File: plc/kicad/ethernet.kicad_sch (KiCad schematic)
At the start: 26 parts, among them U20 W5500, X1 X322525MRB4SI

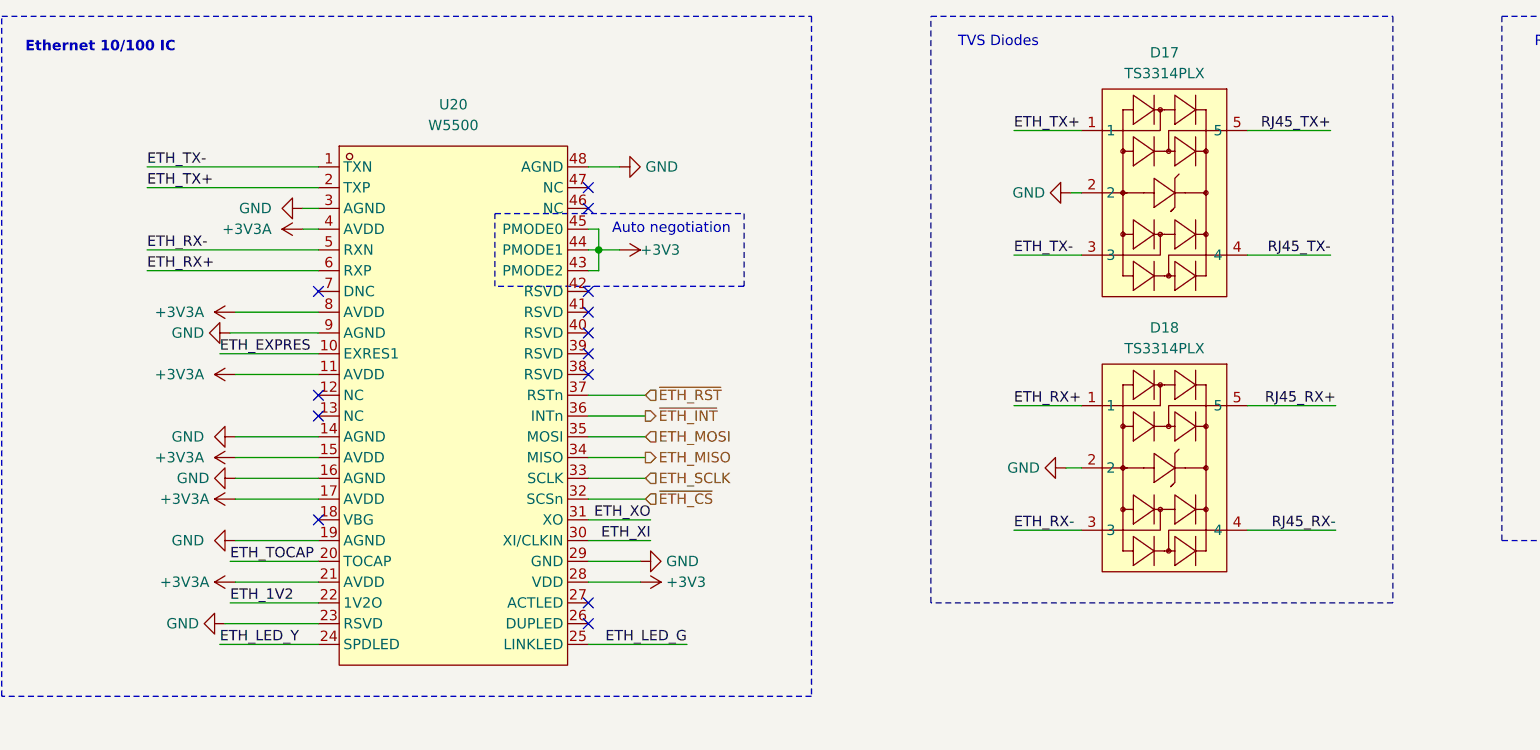
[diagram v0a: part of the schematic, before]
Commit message: Corrected TVS duplicated
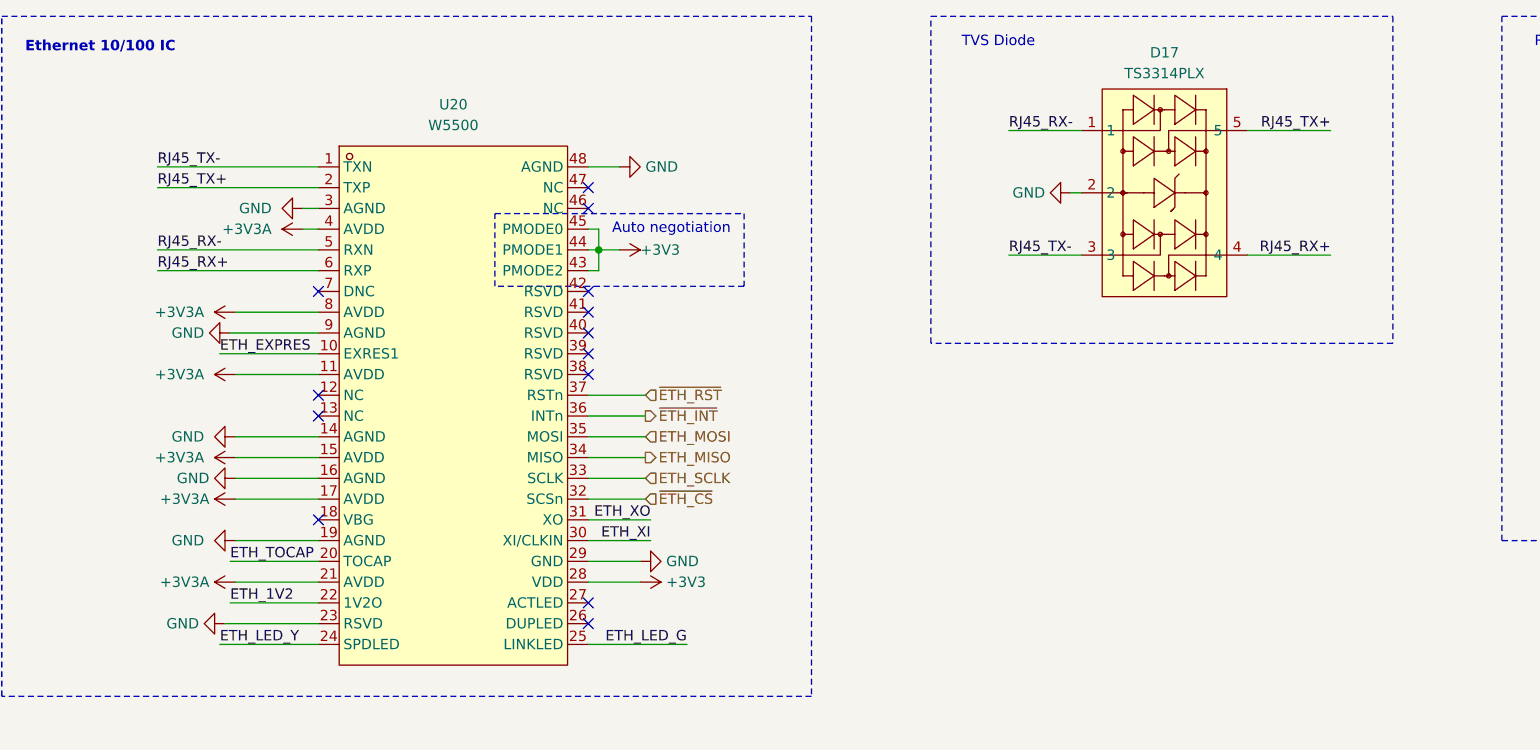
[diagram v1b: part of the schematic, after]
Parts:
- removed D18: TS3314PLX, LibrePLC32:SOT-23-5_L2.9-W1.6-P0.95-LS2.8-BR, symbol LibrePLC32:TS3314PLX
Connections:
- net ETH_RX+ is gone; now on net RJ45_RX+: U20.6 (RXP)
- net ETH_RX- is gone; now on net RJ45_RX-: U20.5 (RXN)
- net ETH_TX- is gone; now on net RJ45_TX-: D17.3, U20.1 (TXN)
- net RJ45_RX+: now also D17.4
- net RJ45_RX-: now also D17.1
- net RJ45_TX+: now also U20.2 (TXP)
- net RJ45_TX-: no longer D17.4
- removed net ETH_TX+: D17.1, U20.2 (TXP)
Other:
- note added: "TVS Diode"
- note removed: "TVS Diodes"

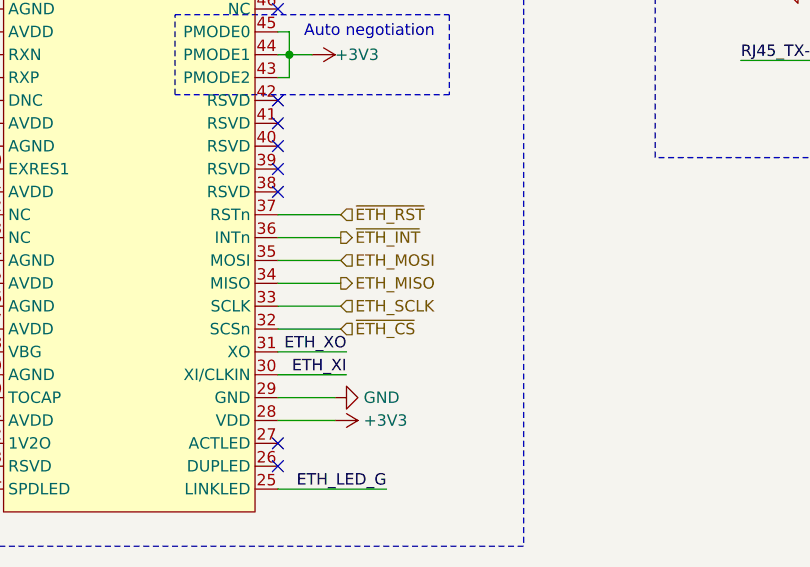
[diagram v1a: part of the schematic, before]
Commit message: Added setup leds & shared SPI bus
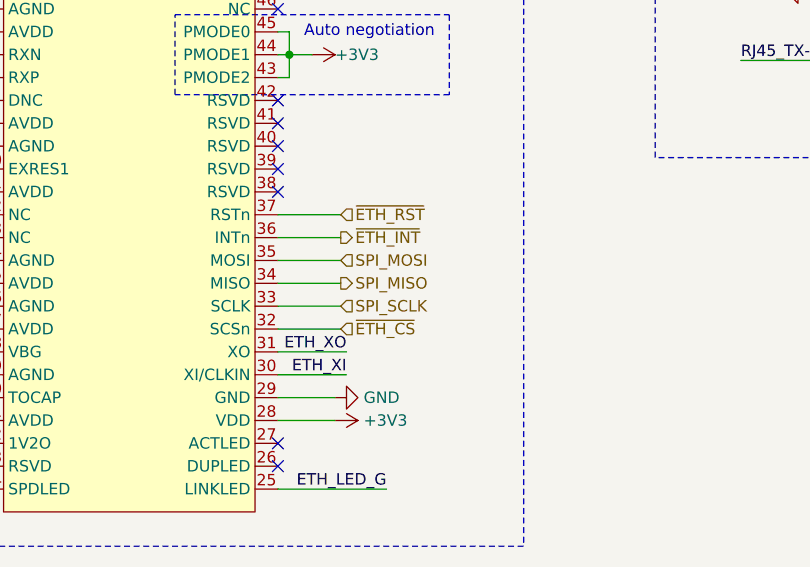
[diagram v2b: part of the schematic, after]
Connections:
- net ETH_MISO renamed SPI_MISO
- net ETH_MOSI renamed SPI_MOSI
- net ETH_SCLK renamed SPI_SCLK
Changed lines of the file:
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@@
 		)
 	)
-	(hierarchical_label "ETH_MOSI"
+	(hierarchical_label "SPI_MOSI"
 		(shape input)
 		(at 99.695 71.12 0)
@@
 		)
 	)
-	(hierarchical_label "ETH_SCLK"
+	(hierarchical_label "SPI_SCLK"
 		(shape input)
 		(at 99.695 76.2 0)
@@
 		)
 	)
-	(hierarchical_label "ETH_MISO"
+	(hierarchical_label "SPI_MISO"
 		(shape output)
 		(at 99.695 73.66 0)

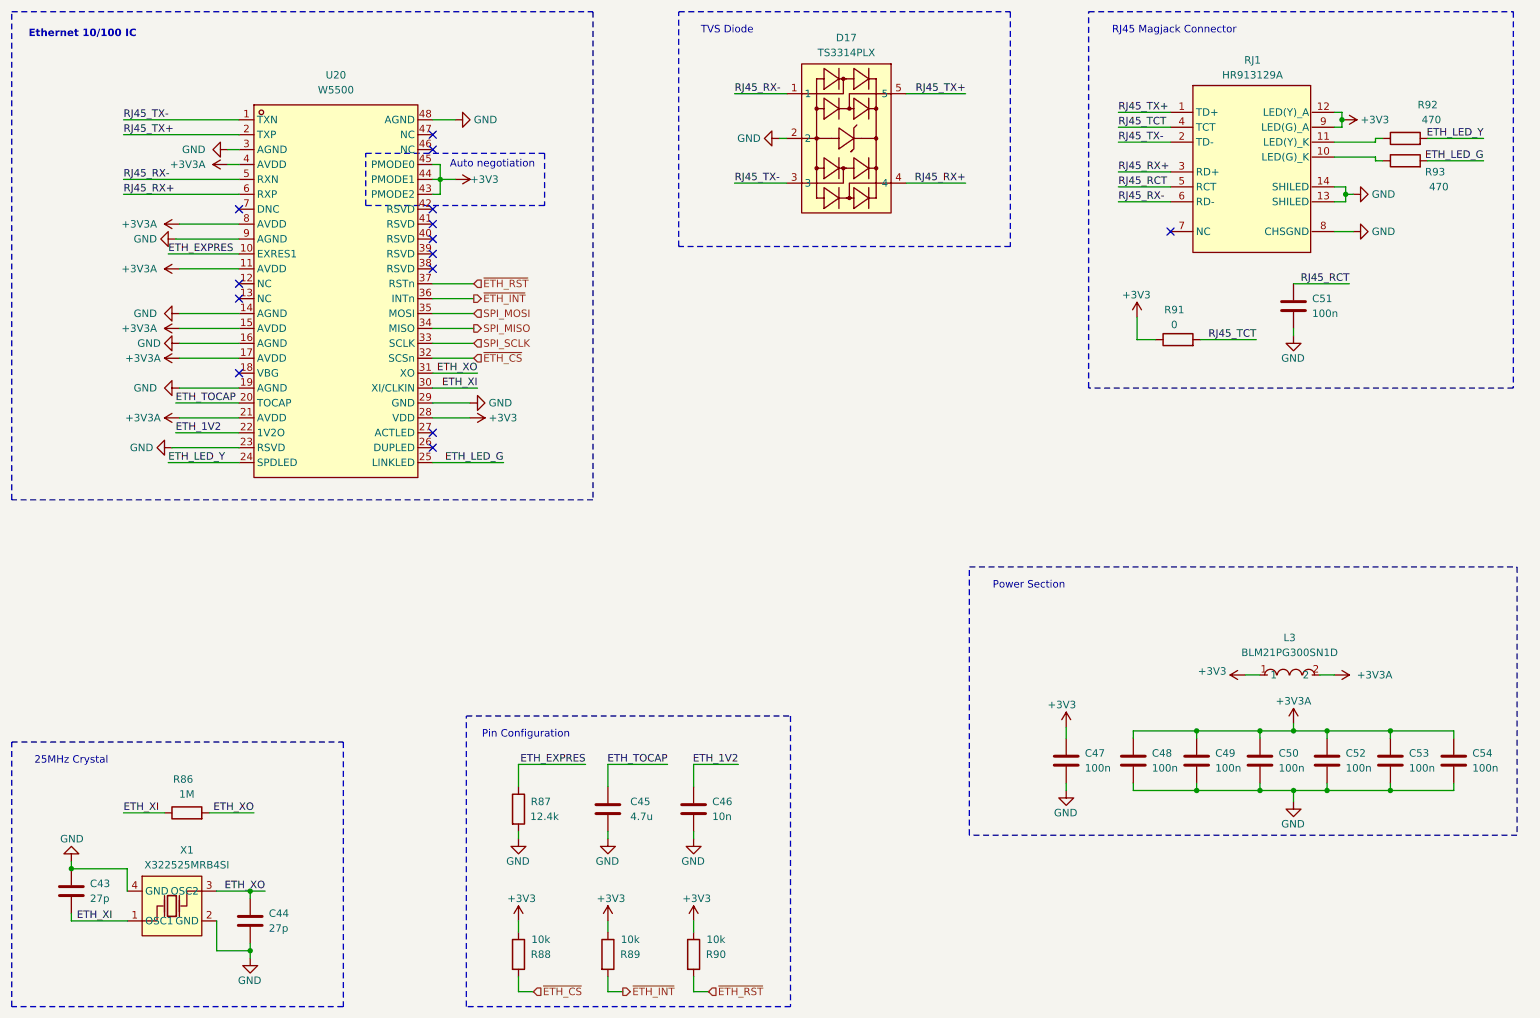
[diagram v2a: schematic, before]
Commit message: Updated W5500 to reference schematic
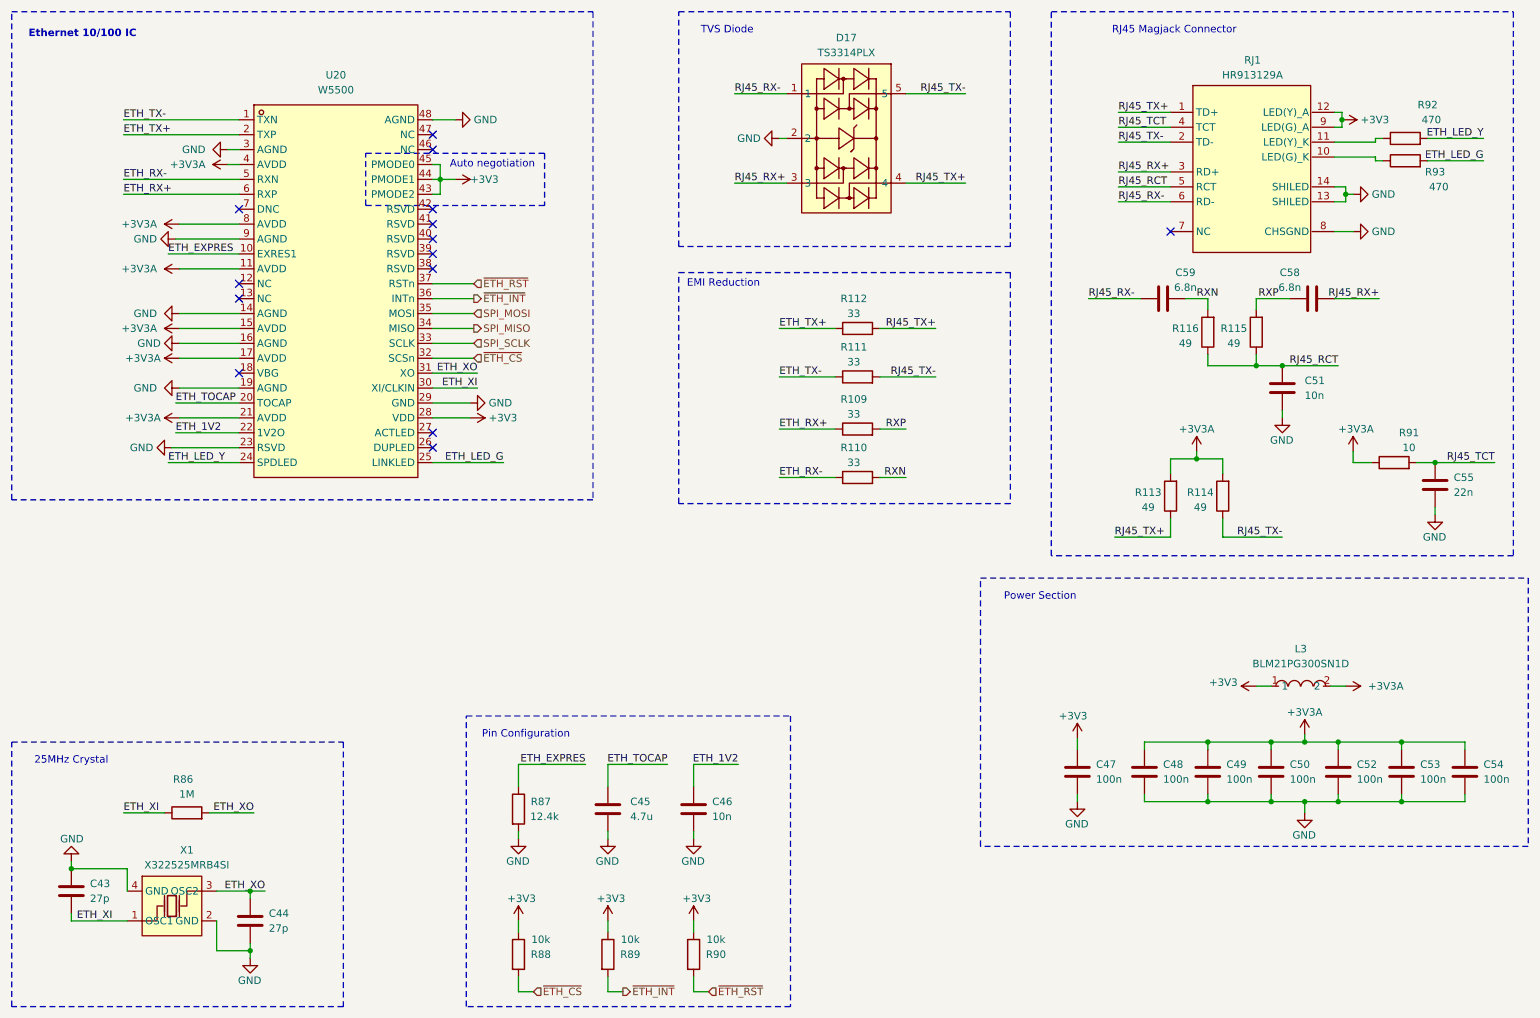
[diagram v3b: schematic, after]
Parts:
- added C55: 22n, Capacitor_SMD:C_0603_1608Metric, symbol Device:C
- added C58, C59: 6.8n, Capacitor_SMD:C_0603_1608Metric, symbol Device:C
- added R109, R110, R111, R112: 33, Resistor_SMD:R_0603_1608Metric, symbol Device:R
- added R113, R114, R115, R116: 49, Resistor_SMD:R_0603_1608Metric, symbol Device:R
- C51: value 100n -> 10n
- R91: value 0 -> 10
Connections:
- net +3V3: no longer R91.1
- net +3V3A: now also R91.1, R113.2, R114.2
- net GND: now also C55.2
- net RJ45_RCT: now also R115.1, R116.1
- net RJ45_RX+: now also D17.3, C58.2; no longer D17.4, U20.6 (RXP)
- net RJ45_RX-: now also C59.2; no longer U20.5 (RXN)
- net RJ45_TCT: now also C55.1
- net RJ45_TX+: now also D17.4, R112.2, R113.1; no longer D17.5, U20.2 (TXP)
- net RJ45_TX-: now also D17.5, R111.2, R114.1; no longer D17.3, U20.1 (TXN)
- new net ETH_RX+: R109.1, U20.6 (RXP)
- new net ETH_RX-: R110.1, U20.5 (RXN)
- new net ETH_TX+: R112.1, U20.2 (TXP)
- new net ETH_TX-: R111.1, U20.1 (TXN)
- new net RXN: C59.1, R110.2, R116.2
- new net RXP: C58.1, R109.2, R115.2
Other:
- note added: "EMI Reduction"
- moved on the sheet: C47, C48, C49, C50, C51, C52, C53, C54, L3, R91

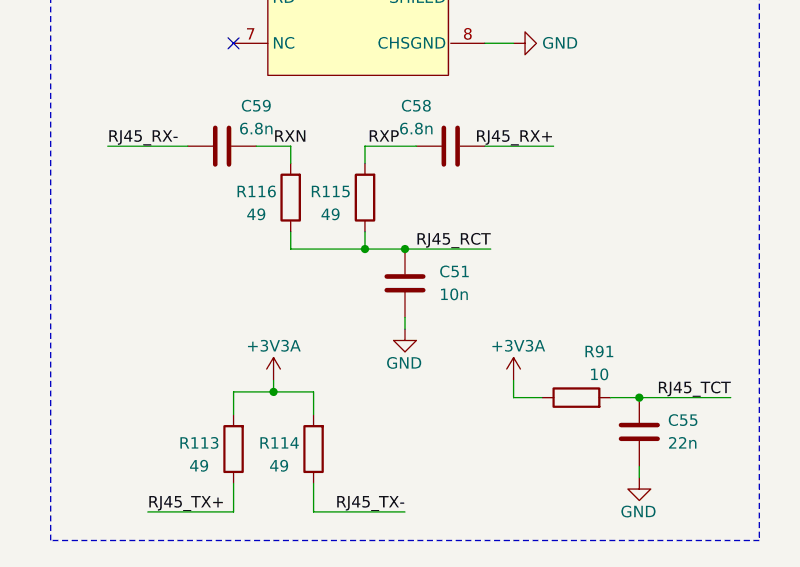
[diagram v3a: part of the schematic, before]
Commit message: SD Card PCB Placement
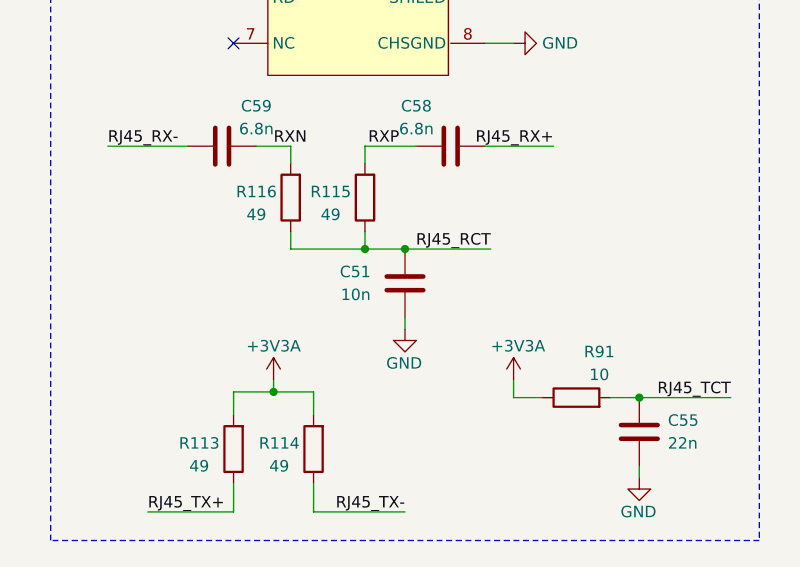
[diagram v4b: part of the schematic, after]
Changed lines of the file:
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@@
 		(lib_id "Device:C")
 		(at 237.49 83.82 0)
+		(mirror y)
 		(unit 1)
 		(body_style 1)
@@
 		(in_pos_files yes)
 		(dnp no)
-		(fields_autoplaced yes)
 		(property "Reference" "C51"
-			(at 241.3 82.5499 0)
+			(at 233.68 82.5499 0)
 			(show_name no)
 			(do_not_autoplace no)
@@
 		)
 		(property "Value" "10n"
-			(at 241.3 85.0899 0)
+			(at 233.68 85.0899 0)
 			(show_name no)
 			(do_not_autoplace no)
@@
 		)
 		(property "Footprint" "Capacitor_SMD:C_0603_1608Metric"
-			(at 238.4552 87.63 0)
+			(at 236.5248 87.63 0)
 			(hide yes)
 			(show_name no)
